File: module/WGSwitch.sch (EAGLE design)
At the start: 26 parts, among them Q1 MMBT3904, Q2 MMBT3904, Q3 MMBT3904, U1 7805TV, U2 ARDUINO_PRO_MINI

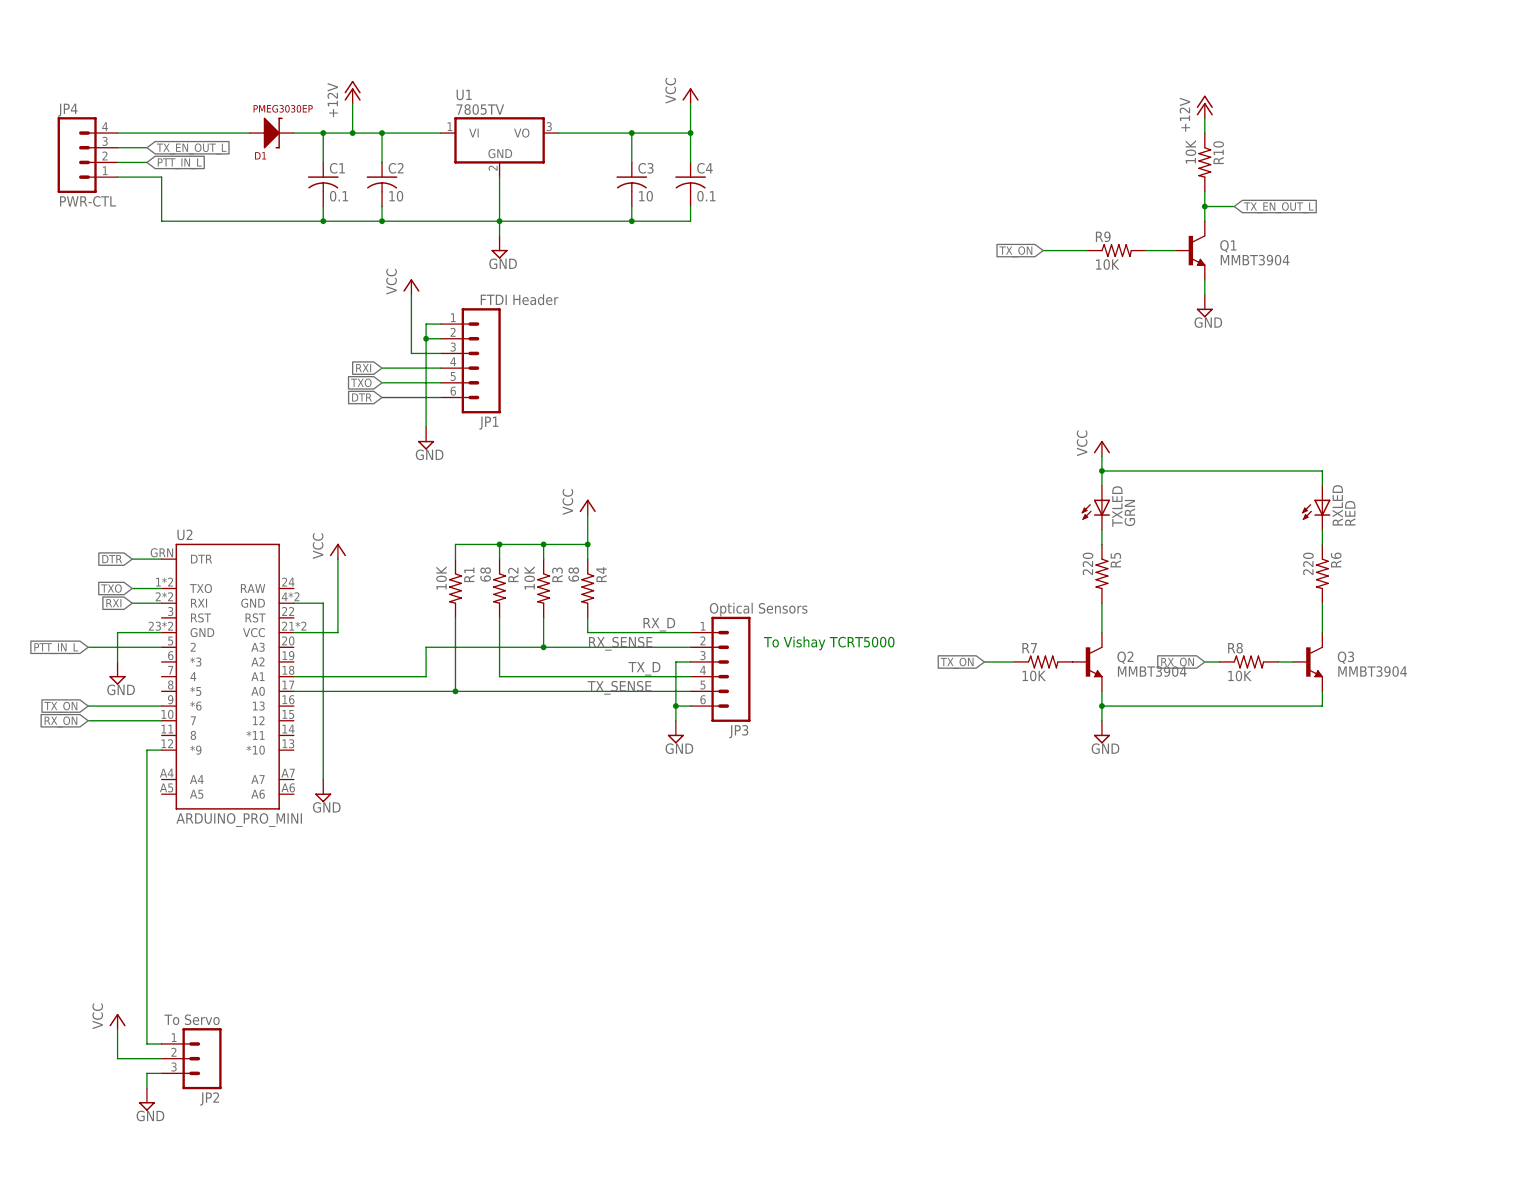
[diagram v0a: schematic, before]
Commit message: cleanup and optimize TRSwitchSleep to eliminate extra delay.
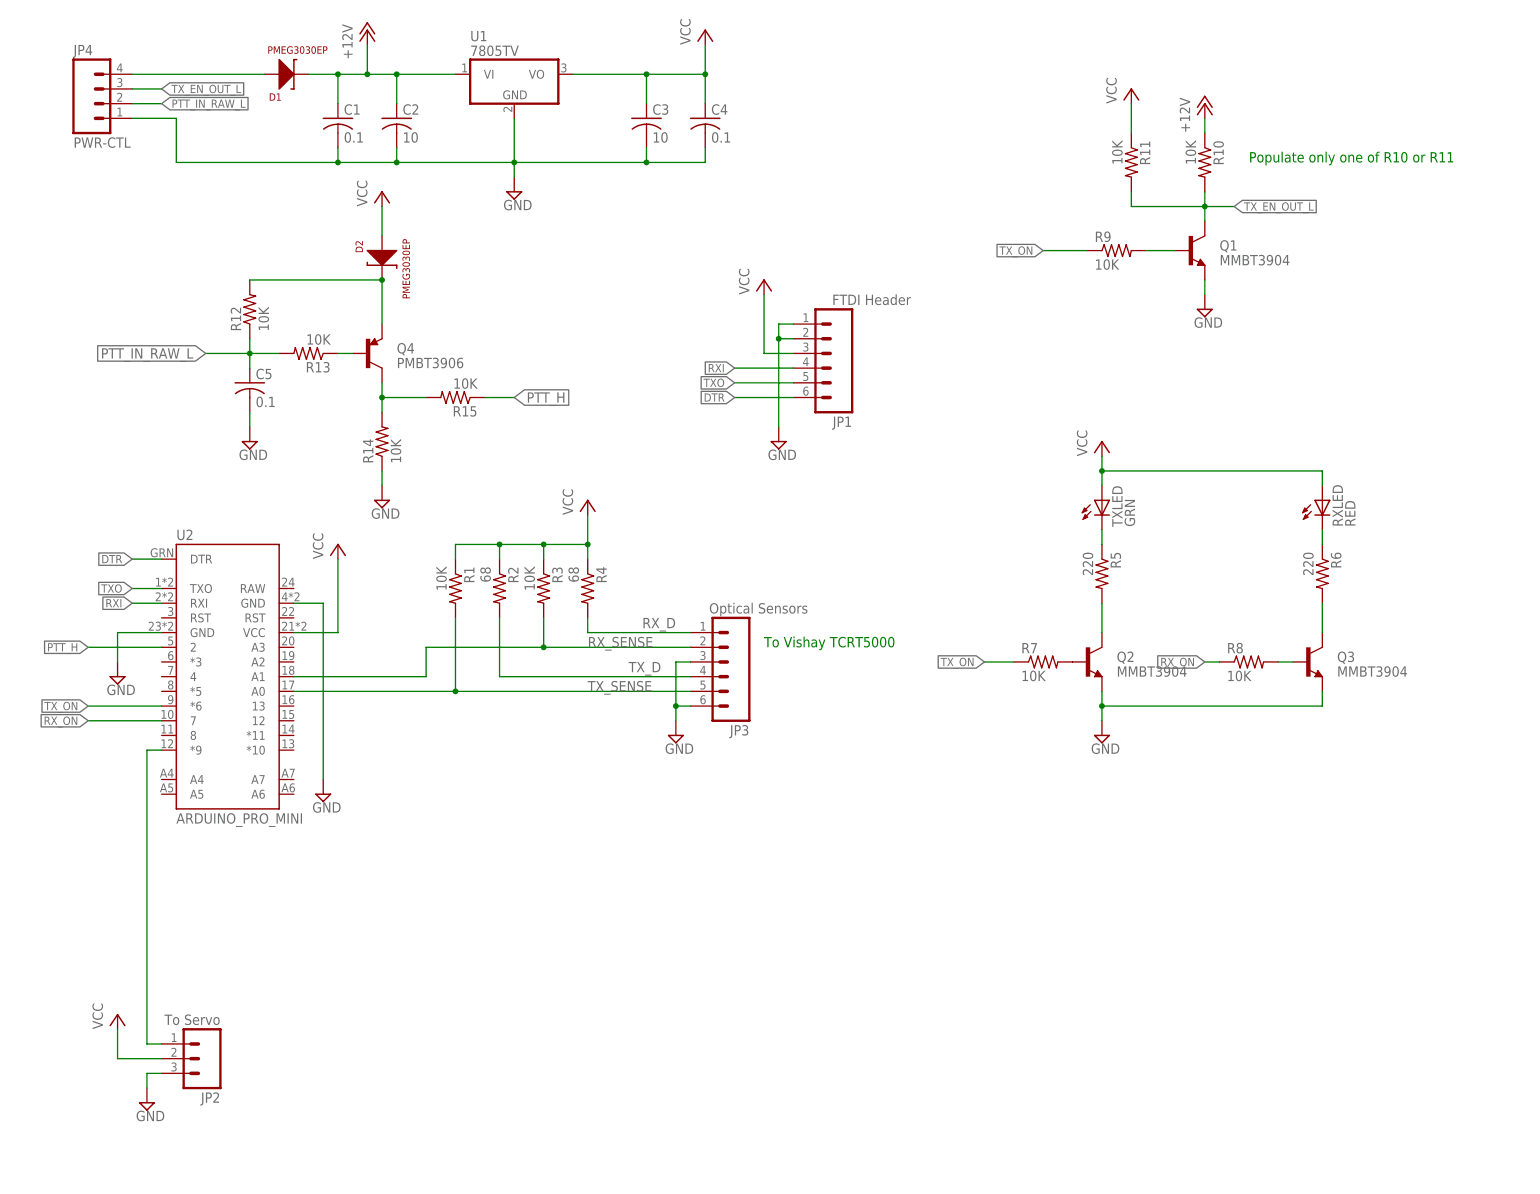
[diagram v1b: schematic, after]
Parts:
- added C5: 0.1, rcl:C-USC0805K
- added D2: PMEG3030EP, kb1vc_robot_parts:PMEG3030EP
- added Q4: PMBT3906, SparkFun-DiscreteSemi:TRANSISTOR_PNPPMBT3906
- added R11, R12, R13, R14, R15: 10K, rcl:R-US_R1206
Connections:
- removed net PTT_IN_L: JP4.2, U2.2
- new net N$12: Q4.C, R14.2, R15.2
- new net N$5: D2.C, Q4.E, R12.2
- new net N$9: Q4.B, R13.1
- new net PTT_H: R15.1, U2.2
- new net PTT_IN_RAW_L: C5.1, JP4.2, R12.1, R13.2
- net GND: now also C5.2, R14.1
- net TX_EN_OUT_L: now also R11.2
- net VCC: now also D2.A, R11.1
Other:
- note added: "Populate only one of R10 or R11"
- moved on the sheet: C1, C2, C3, C4, D1, JP1, JP4, U1

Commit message: Just about right.
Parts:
- removed C5: 0.1, rcl:C-USC0805K
- removed D2: PMEG3030EP, kb1vc_robot_parts:PMEG3030EP
- removed Q4: PMBT3906, SparkFun-DiscreteSemi:TRANSISTOR_PNPPMBT3906
- removed R11, R12, R13, R14, R15: 10K, rcl:R-US_R1206
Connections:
- removed net N$12: Q4.C, R14.2, R15.2
- removed net N$5: D2.C, Q4.E, R12.2
- removed net N$9: Q4.B, R13.1
- removed net PTT_H: R15.1, U2.2
- removed net PTT_IN_RAW_L: C5.1, JP4.2, R12.1, R13.2
- new net PTT_IN_L: JP4.2, U2.2
- net GND: no longer C5.2, R14.1
- net TX_EN_OUT_L: no longer R11.2
- net VCC: no longer D2.A, R11.1
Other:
- note added: "A"
- note added: "Waveguide Switch Servo Controller"
- note removed: "Populate only one of R10 or R11"
- moved on the sheet: C1, C2, C3, C4, D1, JP1, JP4, U1
